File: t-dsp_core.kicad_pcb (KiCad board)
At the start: 4 copper layers, 100 x 61 mm, 164 parts, among them IC1 Logic Level Shifter - 74HCT2G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, J1 J_PWR, J11 J_LED, J12 J_ETH, J13 u.FL DNP (IDC767 ext-antenna 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, J2 J_TDM, J3 J_T, J4 J_USB, J5 J_MIDI, J7 J_SAI2, J8 J_S3, Q1 AO3401A, T108 Tab, T109 Tab, T110 Tab, T111 Tab, U1 Teensy 4.1 - DEVKIT, U11 Dual Buffer - SN74LVC2G125DCTR, U13 ESP32-S3-WROOM-1-N16R8, U15 LT3045EMSE#TRPBF, U19 SN74LVC257APWR, U20 SN74LVC2G125DCTR, U21 SN74LVC244APWR, U22 IDC777-1, U23 SN74LVC138APWR, U24 AP63203WU, U4 Optoisolators - H11L1SM - 6-S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, U5 SN74LVC541APWR, U6 SN74LVC2G125DCTR, U7 SN74LVC2G125DCTR, U9 Dual Buffer - 74HCT2G17GW,125, Y1 24.576MHz

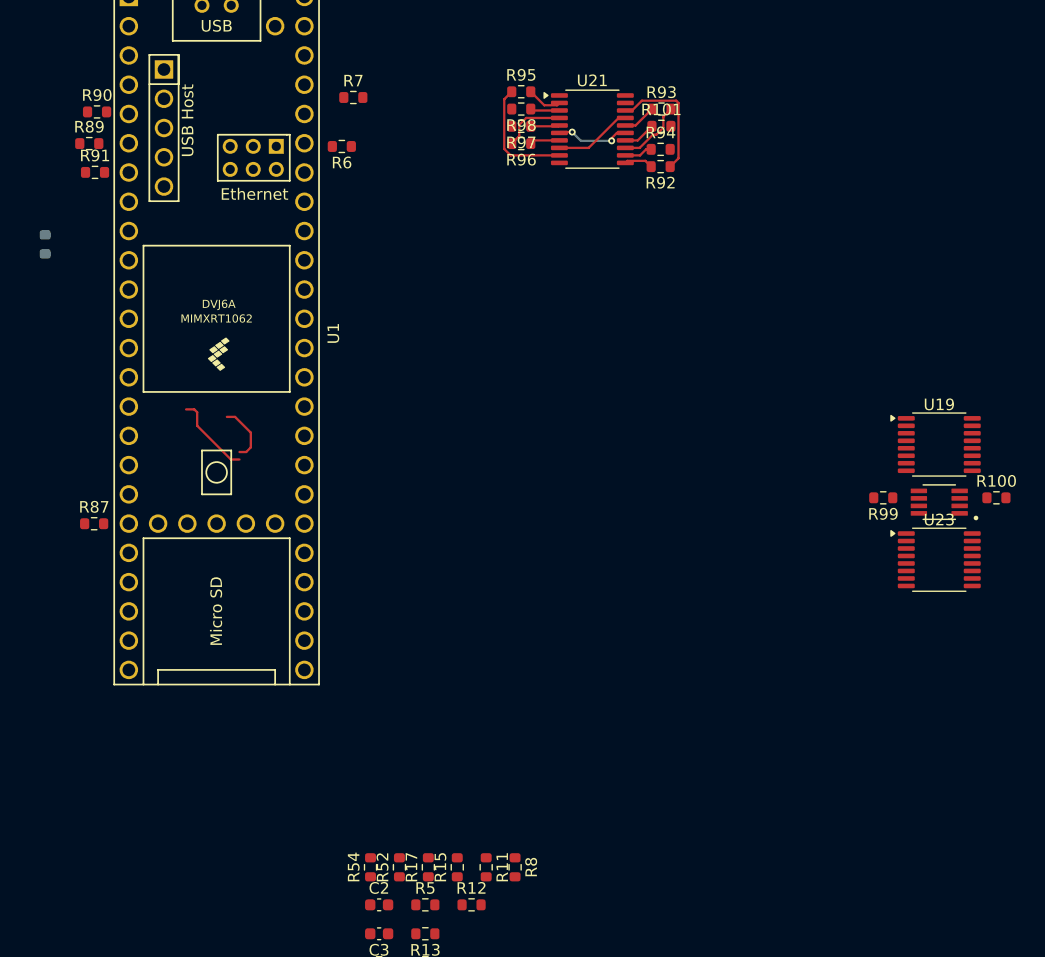
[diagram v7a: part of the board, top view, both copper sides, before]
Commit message: Board: series resistors fanned out beside their driver pins (U19, U20, Teensy pins 23 and 45)
- R89/R90/R91 at U19, R99/R100 at U20, R7 at Teensy pin 45 (MCLK1), R52 at Teensy pin 23: chip-side pad facing the pin, 2.6 mm off the pad (2.75 mm for the Teensy through-hole pins), same side as the chip, with a 0.25 mm stub track.
- U5 and U21 groups were already done by hand and are untouched.
- Not moved: R55/R56/R75/R76/R81 (U11/U6/U7 are stacked too tightly), R3/R4/R6/R9 (host and Ethernet pads sit beside those Teensy pins), R61 (J2 is in the way at Y1), R5 (header series resistor, no driver chip).

Co-Authored-By: Claude Fable 5.1 <noreply@anthropic.com>
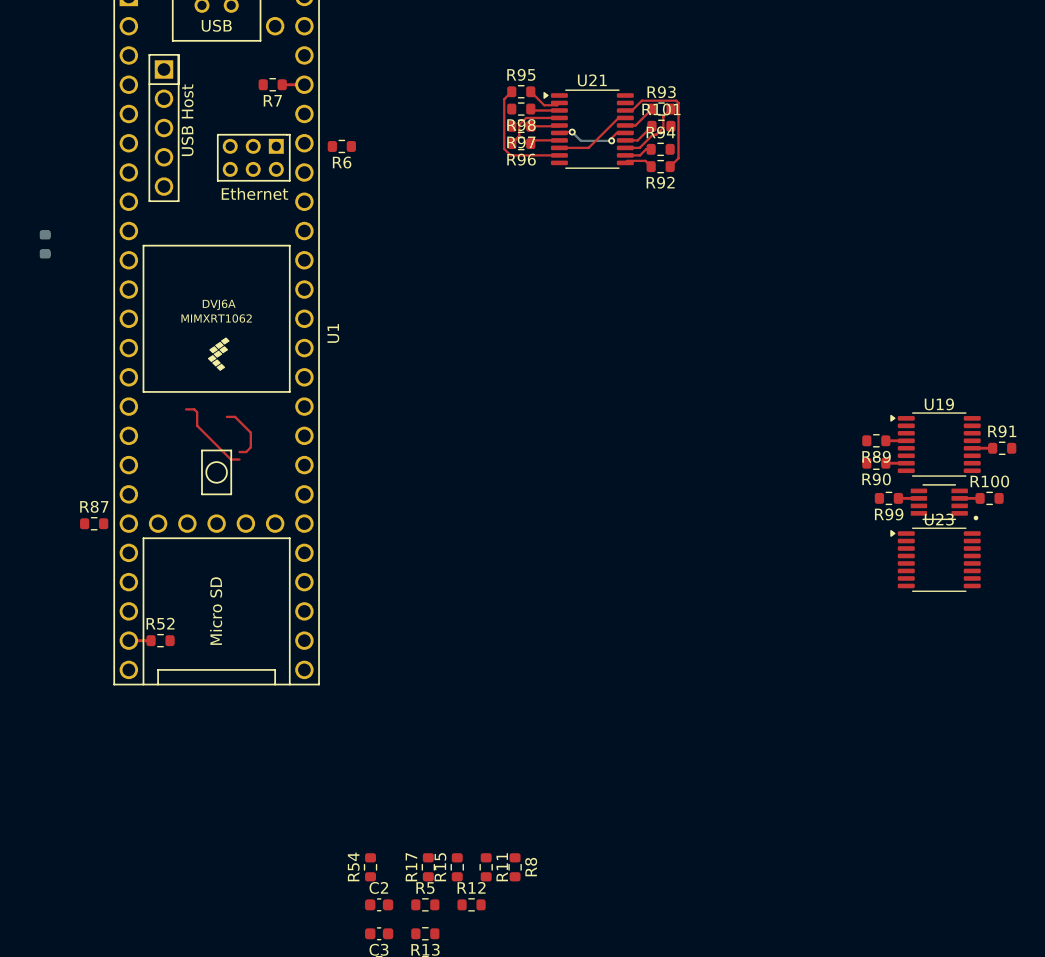
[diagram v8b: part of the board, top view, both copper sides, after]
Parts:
- moved R91 82.3 mm to (295.1, 177.7)
- moved R90 74.2 mm to (284.1, 179.0), turned to 180 degrees
- moved R89 73.0 mm to (284.1, 177.1), turned to 180 degrees
- moved R52 28.6 mm to (222.0, 194.4), turned to 0 degrees
- moved R7 7.09 mm to (231.8, 146.1), turned to 180 degrees
- moved R100 0.59 mm to (294.0, 182.1)
- moved R99 0.50 mm to (285.2, 182.1)
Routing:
- net Net-(U1-31_CTX3): track 0.00 -> 1.93 mm
- net Net-(U1-23_A9_CRX1_MCLK1): track 0.00 -> 1.93 mm
- net Net-(U20-1Y): track 0.00 -> 1.78 mm
- net Net-(U20-2Y): track 0.00 -> 1.78 mm
- net Net-(U19-Zc): track 0.00 -> 1.77 mm
- net Net-(U19-Zb): track 0.00 -> 1.77 mm
- net Net-(U19-Za): track 0.00 -> 1.77 mm
